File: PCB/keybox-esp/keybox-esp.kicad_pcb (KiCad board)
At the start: 2 copper layers, 72 x 31 mm, 3 parts, among them J1 Micro_SD_Card, U1 ESP32-WROVER

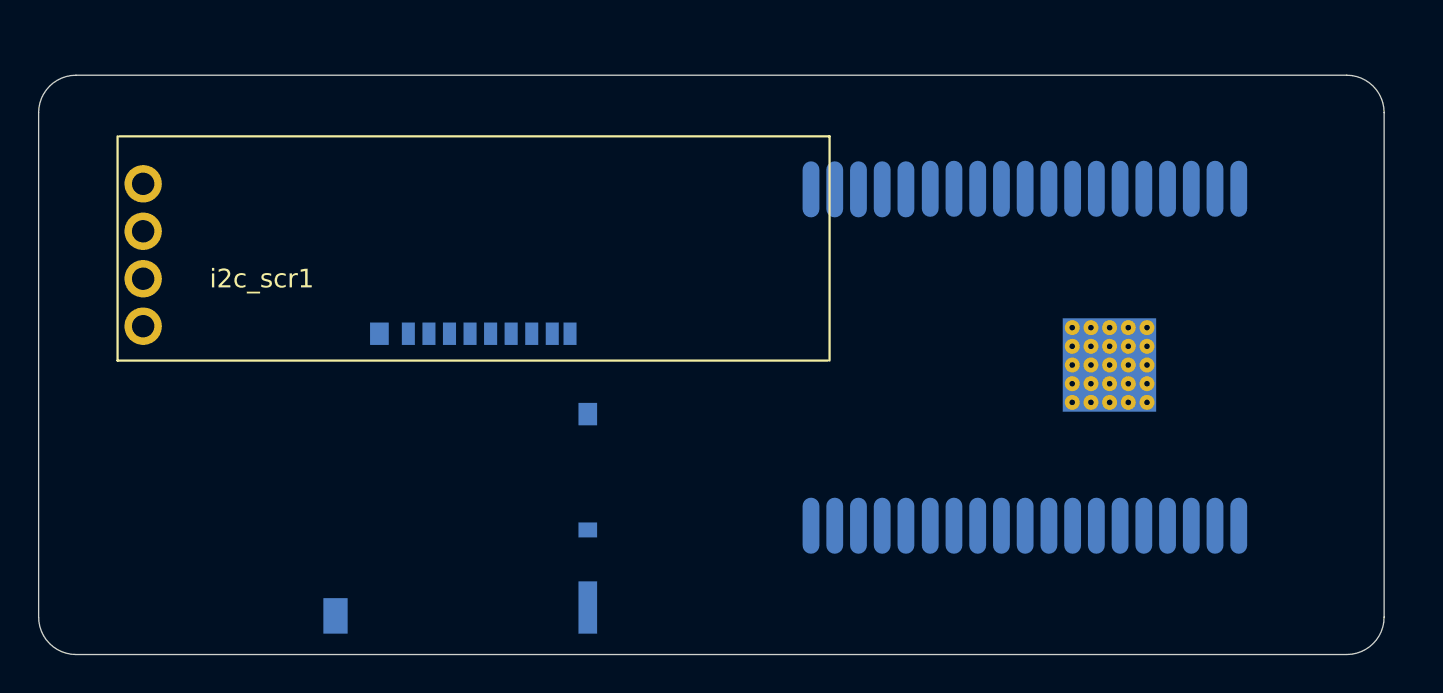
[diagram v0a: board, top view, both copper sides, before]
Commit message: PCB sans wireing ni usb
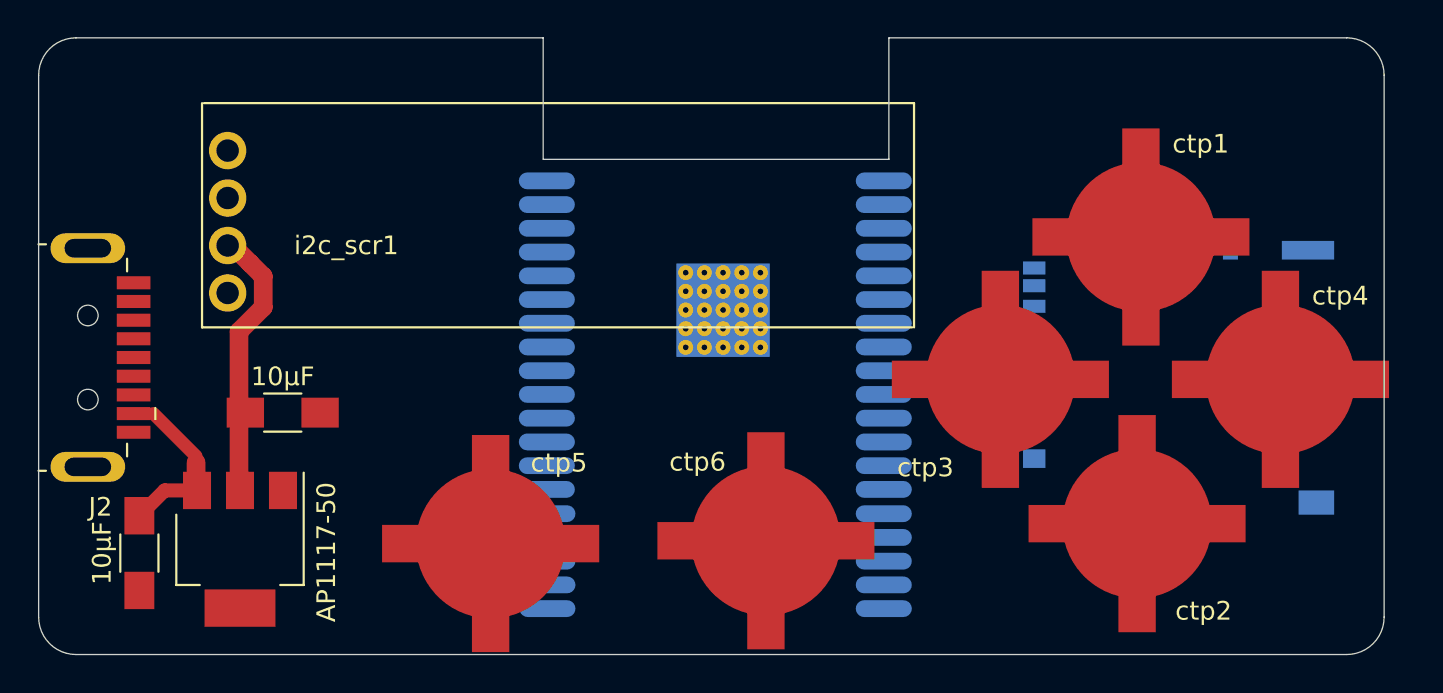
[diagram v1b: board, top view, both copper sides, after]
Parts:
- added C3.3V1: 10µF, AMS1117:C_1206_HandSoldering, F.Cu at (134.1, 124.1)
- added C5V1: 10µF, AMS1117:C_1206_HandSoldering, F.Cu at (126.4, 131.6)
- added J2: USB_A, Connector_USB:USB3_A_Plug_Wuerth_692112030100_Horizontal, F.Cu at (124.3, 121.1)
- added U2: AP1117-50, AMS1117:SOT-223-3Lead_TabPin2, F.Cu at (131.8, 131.4)
- added ctp1: UP, capacitive_touch_pads:simple_pad_solder, F.Cu at (180.0, 114.7)
- added ctp2: DOWN, capacitive_touch_pads:simple_pad_solder, F.Cu at (179.8, 130.0)
- added ctp3: LEFT, capacitive_touch_pads:simple_pad_solder, F.Cu at (172.5, 122.3)
- added ctp4: RIGHT, capacitive_touch_pads:simple_pad_solder, F.Cu at (187.5, 122.3)
- added ctp5: BACK, capacitive_touch_pads:simple_pad_solder, F.Cu at (145.2, 131.1)
- added ctp6: OK, capacitive_touch_pads:simple_pad_solder, F.Cu at (159.9, 130.9)
- moved J1 38.8 mm to (182.0, 122.2), turned to 270 degrees
- moved U1 30.7 mm to (157.2, 110.7), turned to 180 degrees
- moved i2c_scr1 4.86 mm to (131.1, 117.7)
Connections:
- J1 pad 9: Net-(J1-Pad9) -> GND
- U1 pad 13: Net-(U1-Pad13) -> touch_up
- U1 pad 14: Net-(U1-Pad14) -> touch_right
- U1 pad 23: Net-(U1-Pad23) -> touch_left
- U1 pad 24: Net-(U1-Pad24) -> touc_down
- U1 pad 25: Net-(U1-Pad25) -> touch_ok
- U1 pad 26: Net-(U1-Pad26) -> touch_back
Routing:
- net +3V3: track 0.00 -> 14.4 mm
- net +5V: track 0.00 -> 9.76 mm
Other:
- board size 72 x 31 mm -> 72 x 33 mm

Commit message: ajout du ftdi
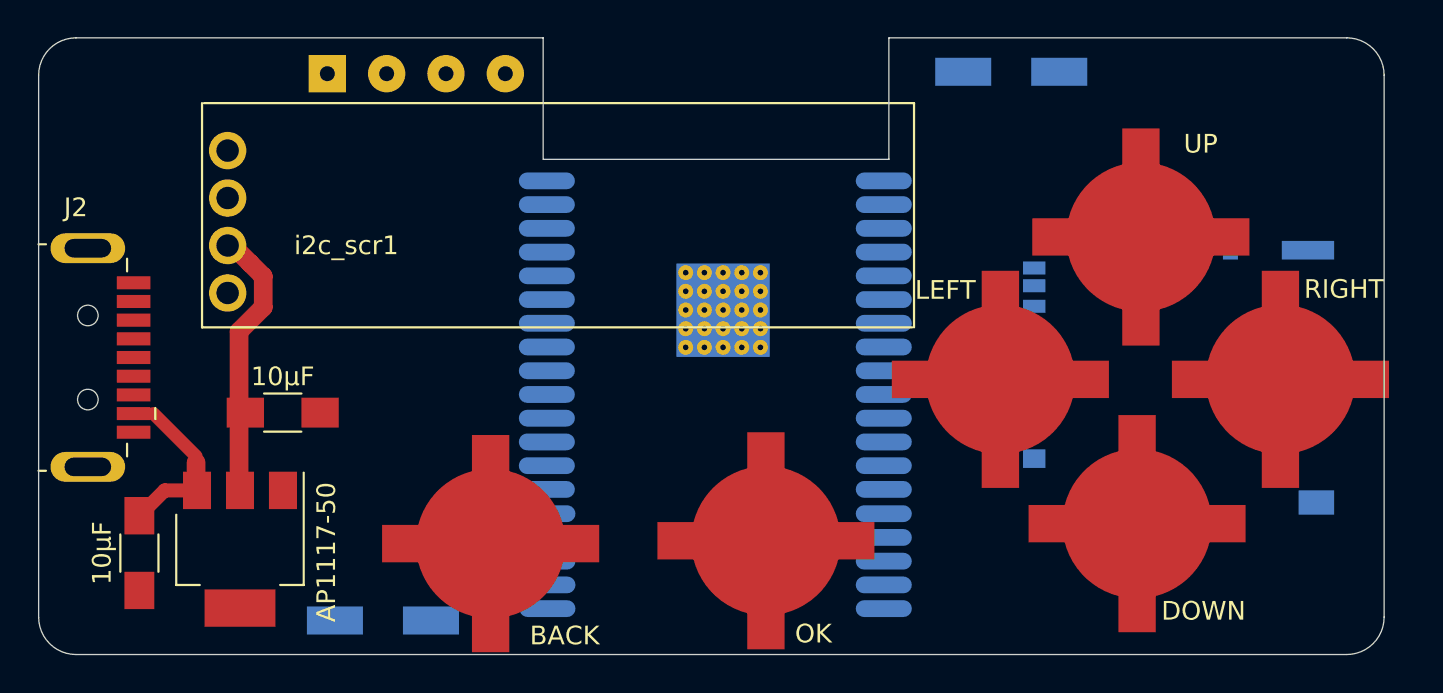
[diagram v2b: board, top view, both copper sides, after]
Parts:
- added FTDI1: FTDI, Connector_Wire:SolderWirePad_1x04_P3.175mm_Drill0.8mm, B.Cu at (136.4, 105.9)
- added flash_jumper1: flash jmp, keybox-esp:jumper_smd, B.Cu at (139.4, 135.2)
- added rst1: rst, keybox-esp:jumper_smd, B.Cu at (173.1, 105.8)
- renumbered ctp5 to BACK, ctp2 to DOWN, ctp3 to LEFT, ctp6 to OK, ctp4 to RIGHT, ctp1 to UP
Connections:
- U1 pad 12: Net-(U1-Pad12) -> touc_down
- U1 pad 24: touc_down -> touch_ok
- U1 pad 25: touch_ok -> flash_jmp
- U1 pad 3: Net-(U1-Pad3) -> esp_reset
- U1 pad 34: Net-(U1-Pad34) -> esp_RX
- U1 pad 35: Net-(U1-Pad35) -> esp_TX

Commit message: ajout de leds RGB
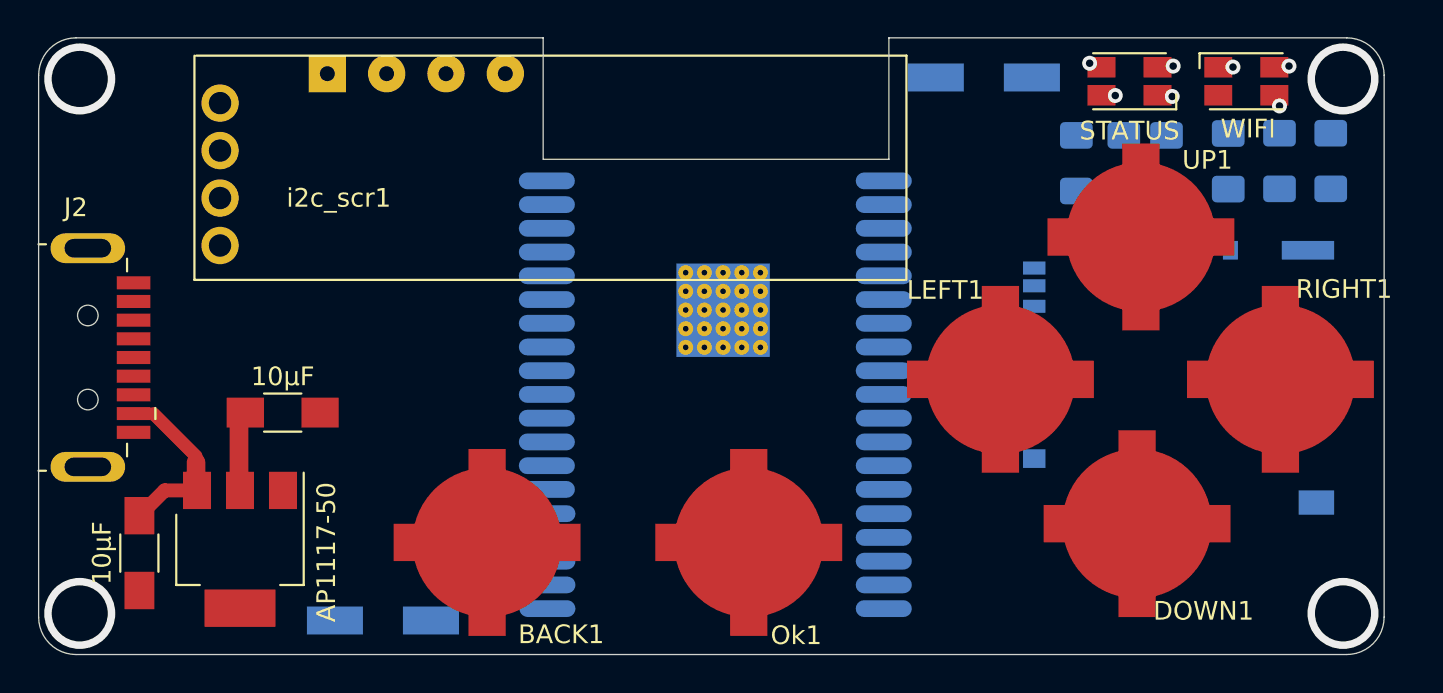
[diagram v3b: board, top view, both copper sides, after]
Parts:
- added RBS1: 150, Resistor_SMD:R_1206_3216Metric_Pad1.42x1.75mm_HandSolder, B.Cu at (176.5, 110.7)
- added RBW1: 150, Resistor_SMD:R_1206_3216Metric_Pad1.42x1.75mm_HandSolder, B.Cu at (187.4, 110.6)
- added RGS1: 150, Resistor_SMD:R_1206_3216Metric_Pad1.42x1.75mm_HandSolder, B.Cu at (179.1, 110.7)
- added RGW1: 150, Resistor_SMD:R_1206_3216Metric_Pad1.42x1.75mm_HandSolder, B.Cu at (190.1, 110.6)
- added RRS1: 150, Resistor_SMD:R_1206_3216Metric_Pad1.42x1.75mm_HandSolder, B.Cu at (181.4, 110.7)
- added RRW1: 150, Resistor_SMD:R_1206_3216Metric_Pad1.42x1.75mm_HandSolder, B.Cu at (184.7, 110.6)
- added STATUS: LED_RGB, LED_SMD:LED_Avago_PLCC4_3.2x2.8mm_CW, F.Cu at (179.4, 106.3)
- added WIFI: LED_RGB, LED_SMD:LED_Avago_PLCC4_3.2x2.8mm_CW, F.Cu at (185.6, 106.3)
- i2c_scr1: value i2c_screen -> SSD1306
- moved i2c_scr1 2.57 mm to (130.7, 115.1)
- moved rst1 1.55 mm to (171.6, 106.1), turned to 270 degrees
- moved Ok1 0.92 mm to (159.0, 131.0)
- moved BACK1 0.20 mm to (145.0, 131.0)
- renumbered BACK to BACK1, DOWN to DOWN1, LEFT to LEFT1, OK to Ok1, RIGHT to RIGHT1, UP to UP1
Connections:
- net scr_scl renamed esp_i2c_scl
- net scr_sda renamed esp_i2c_sda
- U1 pad 4: Net-(U1-Pad4) -> LED_RGB_WB
- U1 pad 5: Net-(U1-Pad5) -> LED_RGB_WG
- U1 pad 6: Net-(U1-Pad6) -> LED_RGB_WR
- U1 pad 7: Net-(U1-Pad7) -> LED_RGB_SR
- U1 pad 8: Net-(U1-Pad8) -> LED_RGB_SG
- U1 pad 9: Net-(U1-Pad9) -> LED_RGB_SB
- i2c_scr1 pad GND: GND -> Net-(i2c_scr1-PadGND)
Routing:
- net +3V3: track 14.4 -> 4.30 mm
- net Net-(LED_STATUS1-Pad3): vias 0 -> 1
- net Net-(LED_STATUS1-Pad2): vias 0 -> 1
- net (no net): vias 0 -> 9
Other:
- rule via_min_size: 0.4 -> 0.45
